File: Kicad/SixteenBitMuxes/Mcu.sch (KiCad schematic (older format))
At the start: 18 parts, among them J10 Key Pad JST XH, J11 LCD JST XH, J12 Bypass Switch JST XH, J7 Boot Reset PinHeader, J9 SWD_PinHeader, U3 STM32F103C8Tx, Y1 8MHz

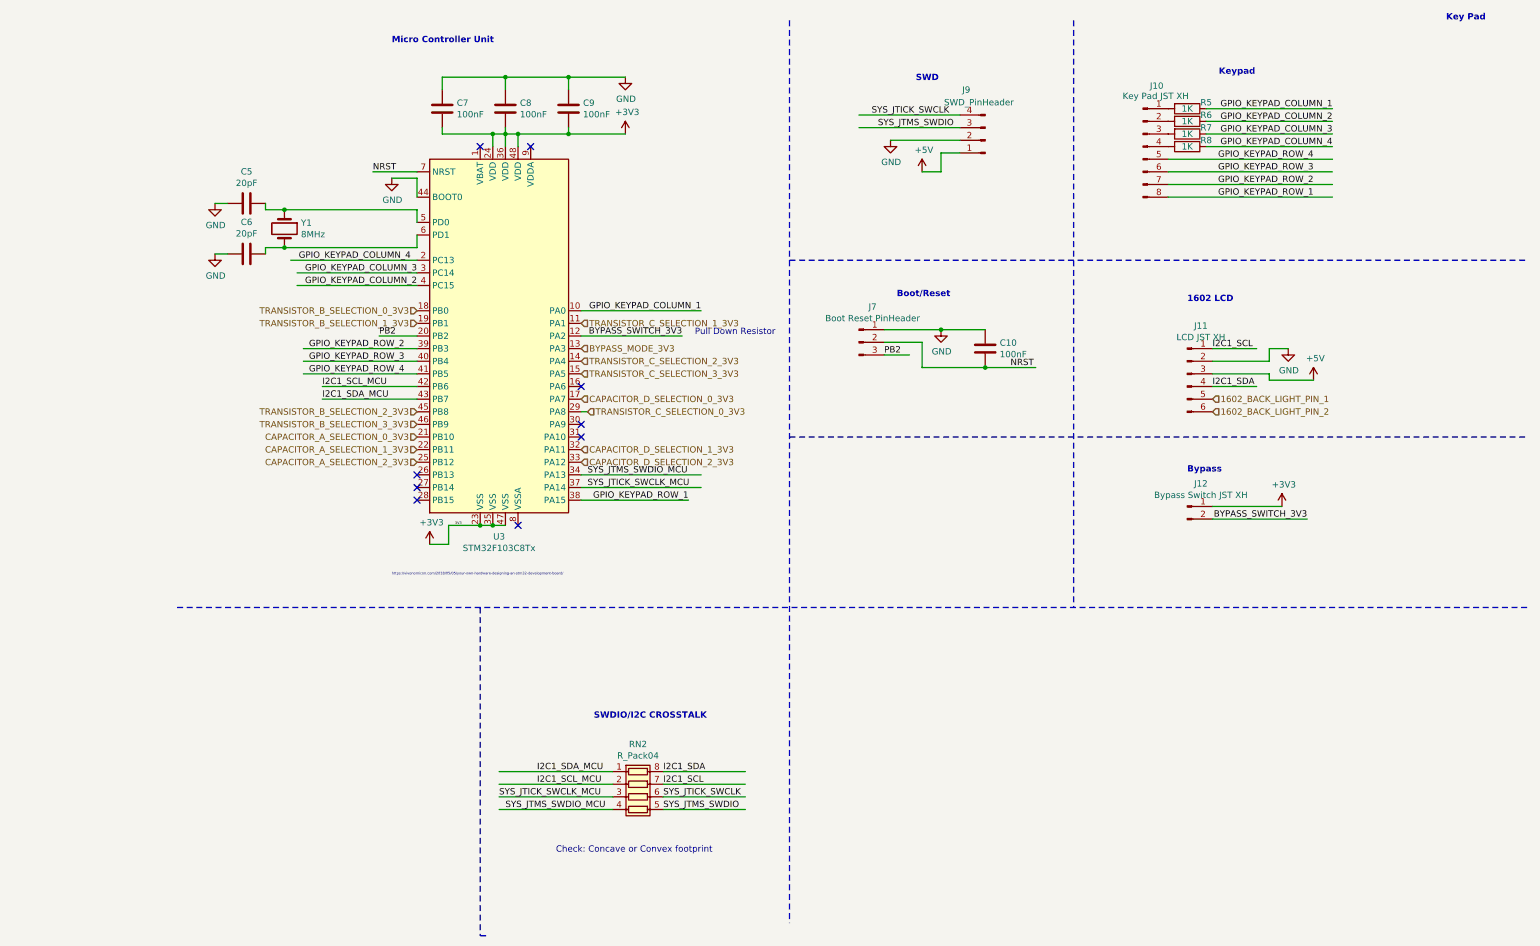
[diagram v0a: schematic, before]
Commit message: LCD backlight and backlight removed from circuit/pcb.
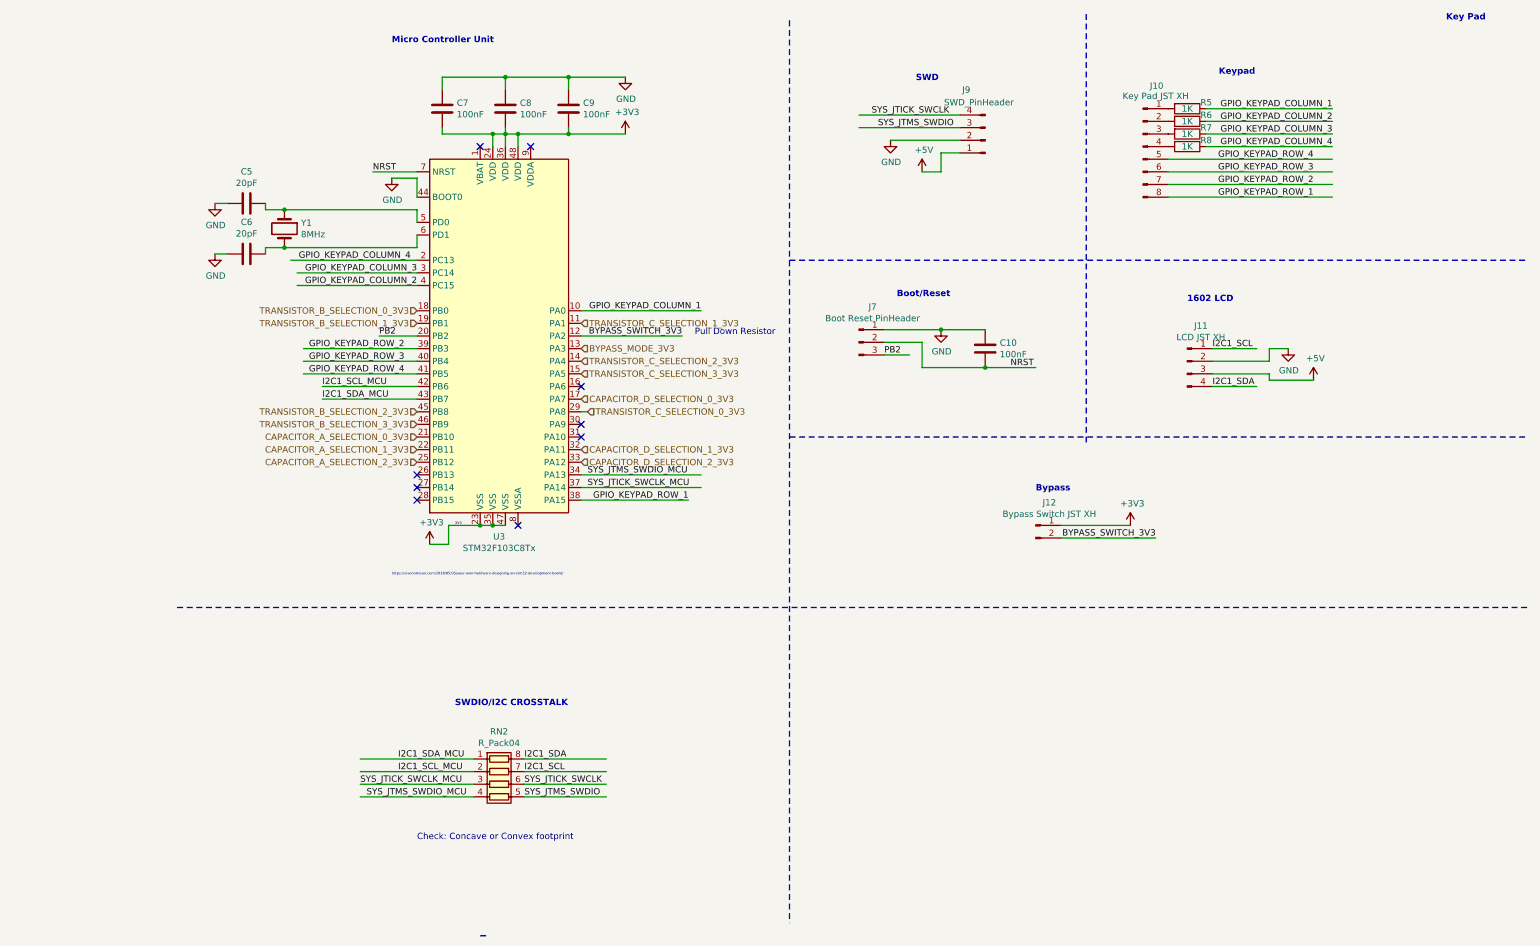
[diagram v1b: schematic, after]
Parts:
- removed J11: LCD JST XH, Connector_JST:JST_XH_B6B-XH-A_1x06_P2.50mm_Vertical, symbol Connector:Conn_01x06_Male
- added J11: LCD JST XH, Connector_JST:JST_XH_B4B-XH-A_1x04_P2.50mm_Vertical, symbol Connector:Conn_01x04_Male
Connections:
- net labels removed: 1602_BACK_LIGHT_PIN_1, 1602_BACK_LIGHT_PIN_2
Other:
- moved on the sheet: J12, RN2
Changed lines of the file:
@@
 Wire Notes Line
 	5350 550  5350 7700
-Wire Notes Line
-	7600 550  7600 5200
 $Comp
 L Device:R R?
@@
 Wire Wire Line
 	9150 3250 9150 3150
-Text Notes 8500 4300 0    50   ~ 10
-Bypass\n\n\n
-$Comp
-L Connector:Conn_01x02_Male J12
-U 1 1 5EBECF25
-P 8500 4400
-F 0 "J12" H 8608 4581 50  0000 C CNN
-F 1 "Bypass Switch JST XH" H 8608 4490 50  0000 C CNN
-F 2 "Connector_JST:JST_XH_B2B-XH-A_1x02_P2.50mm_Vertical" H 8500 4400 50  0001 C CNN
-F 3 "~" H 8500 4400 50  0001 C CNN
-	1    8500 4400
-	1    0    0    -1
-$EndComp
-$Comp
-L Connector:Conn_01x06_Male J11
-U 1 1 5E92561C
-P 8500 3350
-F 0 "J11" H 8608 3731 50  0000 C CNN
-F 1 "LCD JST XH" H 8608 3640 50  0000 C CNN
-F 2 "Connector_JST:JST_XH_B6B-XH-A_1x06_P2.50mm_Vertical" H 8500 3350 50  0001 C CNN
-F 3 "~" H 8500 3350 50  0001 C CNN
-	1    8500 3350
-	1    0    0    -1
-$EndComp
-Text HLabel 8700 3550 2    50   Input ~ 0
-1602_BACK_LIGHT_PIN_1
-Text HLabel 8700 3650 2    50   Input ~ 0
-1602_BACK_LIGHT_PIN_2
-$Comp
-L power:+3V3 #PWR046
-U 1 1 5E9950D9
-P 9250 4400
-F 0 "#PWR046" H 9250 4250 50  0001 C CNN
-F 1 "+3V3" H 9265 4573 50  0000 C CNN
-F 2 "" H 9250 4400 50  0001 C CNN
-F 3 "" H 9250 4400 50  0001 C CNN
-	1    9250 4400
-	1    0    0    -1
-$EndComp
-Wire Wire Line
-	8700 4400 9250 4400
 Text Notes 4600 3050 0    50   ~ 0
 Pull Down Resistor
@@
 Wire Wire Line
 	3700 3050 4500 3050
-Text Label 9450 4500 2    50   ~ 0
-BYPASS_SWITCH_3V3
-Wire Wire Line
-	8700 4500 9450 4500
 Wire Wire Line
 	2400 3350 1500 3350
@@
 Wire Wire Line
 	1650 3450 2400 3450
-$Comp
-L Device:R_Pack04 RN2
-U 1 1 5EA7D58B
-P 4150 6700
-F 0 "RN2" V 3733 6700 50  0000 C CNN
-F 1 "R_Pack04" V 3824 6700 50  0000 C CNN
-F 2 "Resistor_SMD:R_Array_Convex_4x0603" V 4425 6700 50  0001 C CNN
-F 3 "~" H 4150 6700 50  0001 C CNN
-	1    4150 6700
-	0    1    1    0
-$EndComp
-Text Label 3050 6700 0    50   ~ 0
-SYS_JTICK_SWCLK_MCU
-Text Label 4350 6800 0    50   ~ 0
-SYS_JTMS_SWDIO
-Text Label 4350 6700 0    50   ~ 0
-SYS_JTICK_SWCLK
 Wire Wire Line
 	3700 4150 4650 4150
 Wire Wire Line
 	3700 4250 4650 4250
-Wire Wire Line
-	3950 6600 3050 6600
-Wire Wire Line
-	3050 6500 3950 6500
-Text Label 4350 6600 0    50   ~ 0
-I2C1_SCL
-Text Label 4350 6500 0    50   ~ 0
-I2C1_SDA
-Text Notes 3800 6250 0    50   ~ 10
-SWDIO/I2C CROSSTALK\n\n\n
-Wire Notes Line
-	2900 5200 2900 7800
 Wire Notes Line
 	2900 7800 2950 7800
@@
 Text Notes 8750 1150 0    50   ~ 10
 Keypad\n\n\n
-Text Label 3350 6600 0    50   ~ 0
-I2C1_SCL_MCU
-Text Label 3350 6500 0    50   ~ 0
-I2C1_SDA_MCU
-Text Label 3100 6800 0    50   ~ 0
-SYS_JTMS_SWDIO_MCU
-Wire Wire Line
-	4350 6600 5000 6600
-Wire Wire Line
-	4350 6500 5000 6500
-Wire Wire Line
-	4350 6700 5000 6700
-Wire Wire Line
-	4350 6800 5000 6800
-Wire Wire Line
-	3050 6800 3950 6800
-Wire Wire Line
-	3050 6700 3950 6700
 NoConn ~ 3700 3450
 NoConn ~ 3700 3750
 NoConn ~ 3700 3850
 NoConn ~ 2400 4250
-Text Notes 3500 7150 0    50   ~ 0
+NoConn ~ 2400 4350
+$Comp
+L Connector:Conn_01x04_Male J11
+U 1 1 5EA543F3
+P 8500 3250
+F 0 "J11" H 8608 3531 50  0000 C CNN
+F 1 "LCD JST XH" H 8608 3440 50  0000 C CNN
+F 2 "Connector_JST:JST_XH_B4B-XH-A_1x04_P2.50mm_Vertical" H 8500 3250 50  0001 C CNN
+F 3 "~" H 8500 3250 50  0001 C CNN
+	1    8500 3250
+	1    0    0    -1
+$EndComp
+$Comp
+L Device:R_Pack04 RN2
+U 1 1 5EA7D58B
+P 3050 6600
+F 0 "RN2" V 2633 6600 50  0000 C CNN
+F 1 "R_Pack04" V 2724 6600 50  0000 C CNN
+F 2 "Resistor_SMD:R_Array_Convex_4x0603" V 3325 6600 50  0001 C CNN
+F 3 "~" H 3050 6600 50  0001 C CNN
+	1    3050 6600
+	0    1    1    0
+$EndComp
+Text Label 1950 6600 0    50   ~ 0
+SYS_JTICK_SWCLK_MCU
+Text Label 3250 6700 0    50   ~ 0
+SYS_JTMS_SWDIO
+Text Label 3250 6600 0    50   ~ 0
+SYS_JTICK_SWCLK
+Wire Wire Line
+	2850 6500 1950 6500
+Wire Wire Line
+	1950 6400 2850 6400
+Text Label 3250 6500 0    50   ~ 0
+I2C1_SCL
+Text Label 3250 6400 0    50   ~ 0
+I2C1_SDA
+Text Notes 2700 6150 0    50   ~ 10
+SWDIO/I2C CROSSTALK\n\n\n
+Text Label 2250 6500 0    50   ~ 0
+I2C1_SCL_MCU
+Text Label 2250 6400 0    50   ~ 0
+I2C1_SDA_MCU
+Text Label 2000 6700 0    50   ~ 0
+SYS_JTMS_SWDIO_MCU
+Wire Wire Line
+	3250 6500 3900 6500
+Wire Wire Line
+	3250 6400 3900 6400
+Wire Wire Line
+	3250 6600 3900 6600
+Wire Wire Line
+	3250 6700 3900 6700
+Wire Wire Line
+	1950 6700 2850 6700
+Wire Wire Line
+	1950 6600 2850 6600
+Text Notes 2400 7050 0    50   ~ 0
 Check: Concave or Convex footprint
-NoConn ~ 2400 4350
+Wire Notes Line
+	7700 500  7700 3900
+Text Notes 7300 4450 0    50   ~ 10
+Bypass\n\n\n
+$Comp
+L Connector:Conn_01x02_Male J12
+U 1 1 5EBECF25
+P 7300 4550
+F 0 "J12" H 7408 4731 50  0000 C CNN
+F 1 "Bypass Switch JST XH" H 7408 4640 50  0000 C CNN
+F 2 "Connector_JST:JST_XH_B2B-XH-A_1x02_P2.50mm_Vertical" H 7300 4550 50  0001 C CNN
+F 3 "~" H 7300 4550 50  0001 C CNN
+	1    7300 4550
+	1    0    0    -1
+$EndComp
+$Comp
+L power:+3V3 #PWR046
+U 1 1 5E9950D9
+P 8050 4550
+F 0 "#PWR046" H 8050 4400 50  0001 C CNN
+F 1 "+3V3" H 8065 4723 50  0000 C CNN
+F 2 "" H 8050 4550 50  0001 C CNN
+F 3 "" H 8050 4550 50  0001 C CNN
+	1    8050 4550
+	1    0    0    -1
+$EndComp
+Wire Wire Line
+	7500 4550 8050 4550
+Text Label 8250 4650 2    50   ~ 0
+BYPASS_SWITCH_3V3
+Wire Wire Line
+	7500 4650 8250 4650
 $EndSCHEMATC

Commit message: EEprom + PCB changes
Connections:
- no-connect marks 9 -> 10
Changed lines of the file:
@@
 Text HLabel 3700 3550 2    50   Input ~ 0
 CAPACITOR_D_SELECTION_0_3V3
-Text HLabel 3700 3950 2    50   Input ~ 0
+Text HLabel 3700 3750 2    50   Input ~ 0
 CAPACITOR_D_SELECTION_1_3V3
-Text HLabel 3700 4050 2    50   Input ~ 0
+Text HLabel 3700 3850 2    50   Input ~ 0
 CAPACITOR_D_SELECTION_2_3V3
 Wire Wire Line
@@
 Keypad\n\n\n
 NoConn ~ 3700 3450
-NoConn ~ 3700 3750
-NoConn ~ 3700 3850
 NoConn ~ 2400 4250
 NoConn ~ 2400 4350
@@
 Wire Wire Line
 	7500 4650 8250 4650
+NoConn ~ 3700 3950
+NoConn ~ 3700 4050
+NoConn ~ -800 2650
 $EndSCHEMATC

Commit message: PCB mostly
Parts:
- removed J10: Key Pad JST XH, Connector_JST:JST_XH_B8B-XH-A_1x08_P2.50mm_Vertical, symbol Connector:Conn_01x08_Male
- removed R8: 1K, Resistor_SMD:R_0805_2012Metric_Pad1.15x1.40mm_HandSolder, symbol Device:R
- added J10: JST XH Buttons, Connector_JST:JST_XH_B6B-XH-A_1x06_P2.50mm_Vertical, symbol Connector:Conn_01x06_Male
- added R?: 10K, Resistor_SMD:R_0805_2012Metric_Pad1.15x1.40mm_HandSolder, symbol Device:R
- R5, R6, R7: value 1K -> 10K
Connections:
- net labels added: GPIO_BUTTON_DECREASE, GPIO_BUTTON_ENTER, GPIO_BUTTON_INCREASE
- net labels removed: GPIO_KEYPAD_COLUMN_1, GPIO_KEYPAD_COLUMN_2, GPIO_KEYPAD_COLUMN_3, GPIO_KEYPAD_COLUMN_4, GPIO_KEYPAD_ROW_1, GPIO_KEYPAD_ROW_2, GPIO_KEYPAD_ROW_3, GPIO_KEYPAD_ROW_4
- wire segments 89 -> 93
- no-connect marks 10 -> 15
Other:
- note added: "Buttons\n\n\n\n"
- note added: "See MicroCap ThreeSwitches"
- note removed: "Key Pad\n\n\n\n"
- note removed: "Keypad\n\n\n"
- moved on the sheet: J12, R5, R6, R7
